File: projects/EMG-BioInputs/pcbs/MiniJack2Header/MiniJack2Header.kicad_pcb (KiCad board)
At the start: 2 copper layers, 22.1 x 14 mm, 2 parts, among them J1 SWITCHCRAFT_35RASMT2BHNTRX, J2 901210124

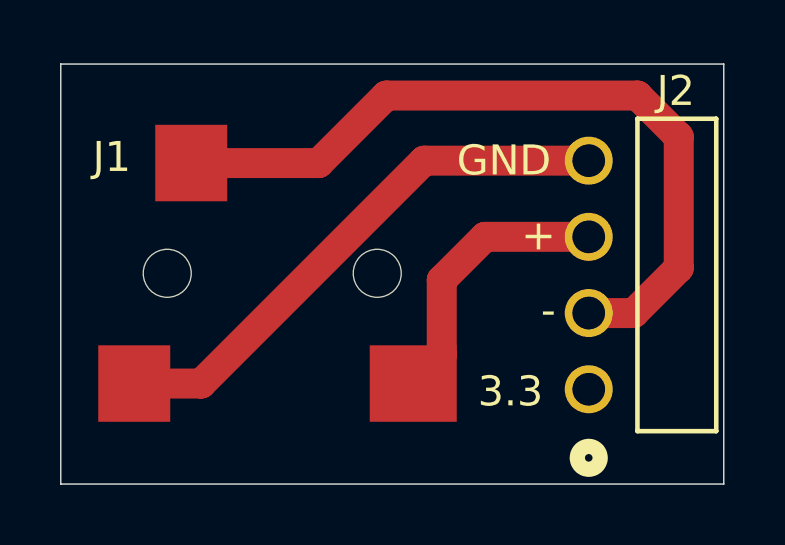
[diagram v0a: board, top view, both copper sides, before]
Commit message: refactor: Rename EMG PCB adapter to Header
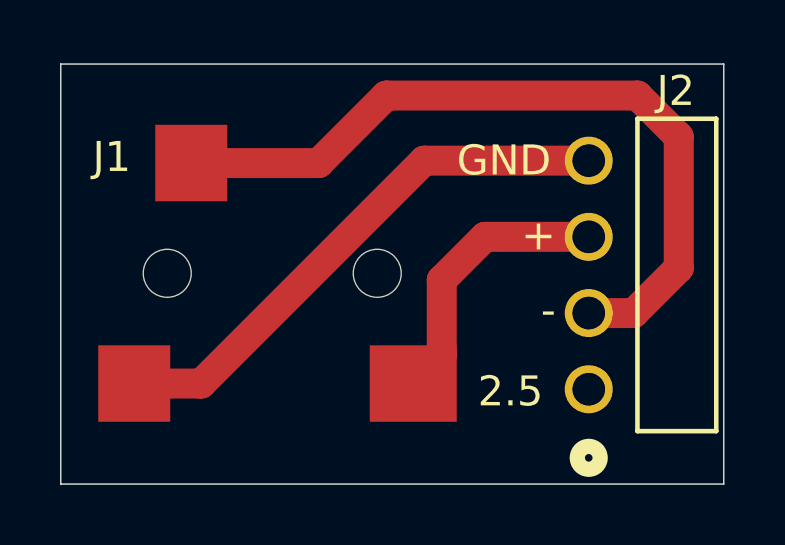
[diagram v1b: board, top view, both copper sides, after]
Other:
- board text added: "2.5"
- board text removed: "3.3"
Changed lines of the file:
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@@
 (kicad_pcb
-	(version 20240108)
+	(version 20241229)
 	(generator "pcbnew")
-	(generator_version "8.0")
+	(generator_version "9.0")
 	(general
 		(thickness 1.6)
@@
 	(layers
 		(0 "F.Cu" signal)
-		(31 "B.Cu" signal)
-		(32 "B.Adhes" user "B.Adhesive")
-		(33 "F.Adhes" user "F.Adhesive")
-		(34 "B.Paste" user)
-		(35 "F.Paste" user)
-		(36 "B.SilkS" user "B.Silkscreen")
-		(37 "F.SilkS" user "F.Silkscreen")
-		(38 "B.Mask" user)
-		(39 "F.Mask" user)
-		(40 "Dwgs.User" user "User.Drawings")
-		(41 "Cmts.User" user "User.Comments")
-		(42 "Eco1.User" user "User.Eco1")
-		(43 "Eco2.User" user "User.Eco2")
-		(44 "Edge.Cuts" user)
-		(45 "Margin" user)
-		(46 "B.CrtYd" user "B.Courtyard")
-		(47 "F.CrtYd" user "F.Courtyard")
-		(48 "B.Fab" user)
-		(49 "F.Fab" user)
-		(50 "User.1" user)
-		(51 "User.2" user)
-		(52 "User.3" user)
-		(53 "User.4" user)
-		(54 "User.5" user)
-		(55 "User.6" user)
-		(56 "User.7" user)
-		(57 "User.8" user)
-		(58 "User.9" user)
+		(2 "B.Cu" signal)
+		(9 "F.Adhes" user "F.Adhesive")
+		(11 "B.Adhes" user "B.Adhesive")
+		(13 "F.Paste" user)
+		(15 "B.Paste" user)
+		(5 "F.SilkS" user "F.Silkscreen")
+		(7 "B.SilkS" user "B.Silkscreen")
+		(1 "F.Mask" user)
+		(3 "B.Mask" user)
+		(17 "Dwgs.User" user "User.Drawings")
+		(19 "Cmts.User" user "User.Comments")
+		(21 "Eco1.User" user "User.Eco1")
+		(23 "Eco2.User" user "User.Eco2")
+		(25 "Edge.Cuts" user)
+		(27 "Margin" user)
+		(31 "F.CrtYd" user "F.Courtyard")
+		(29 "B.CrtYd" user "B.Courtyard")
+		(35 "F.Fab" user)
+		(33 "B.Fab" user)
+		(39 "User.1" user)
+		(41 "User.2" user)
+		(43 "User.3" user)
+		(45 "User.4" user)
+		(47 "User.5" user)
+		(49 "User.6" user)
+		(51 "User.7" user)
+		(53 "User.8" user)
+		(55 "User.9" user)
 	)
 	(setup
@@
 		(pad_to_mask_clearance 0)
 		(allow_soldermask_bridges_in_footprints no)
+		(tenting front back)
 		(pcbplotparams
-			(layerselection 0x00010fc_ffffffff)
-			(plot_on_all_layers_selection 0x0000000_00000000)
+			(layerselection 0x00000000_00000000_55555555_5755f5ff)
+			(plot_on_all_layers_selection 0x00000000_00000000_00000000_00000000)
 			(disableapertmacros no)
 			(usegerberextensions no)
@@
 			(svgprecision 4)
 			(plotframeref no)
-			(viasonmask no)
 			(mode 1)
 			(useauxorigin no)
@@
 			(pdf_front_fp_property_popups yes)
 			(pdf_back_fp_property_popups yes)
+			(pdf_metadata yes)
+			(pdf_single_document no)
 			(dxfpolygonmode yes)
 			(dxfimperialunits yes)
@@
 			(psnegative no)
 			(psa4output no)
-			(plotreference yes)
-			(plotvalue yes)
-			(plotfptext yes)
-			(plotinvisibletext no)
+			(plot_black_and_white yes)
 			(sketchpadsonfab no)
+			(plotpadnumbers no)
+			(hidednponfab no)
+			(sketchdnponfab yes)
+			(crossoutdnponfab yes)
 			(subtractmaskfromsilk no)
 			(outputformat 1)
@@
 			)
 		)
-		(property "Footprint" "MiniJack2Jumper:35RASMT2BHNTRX"
-			(at 0 0 0)
-			(layer "F.Fab")
-			(hide yes)
-			(effects
-				(font
-					(size 1.27 1.27)
-					(thickness 0.15)
-				)
-			)
-		)
 		(property "Datasheet" ""
 			(at 0 0 0)
@@
 				(type default)
 			)
-			(fill none)
+			(fill no)
 			(layer "F.CrtYd")
 		)
@@
 			(size 1.6 1.6)
 			(drill 1.6)
-			(layers "*.Cu" "*.Mask" "In1.Cu" "In2.Cu" "In3.Cu" "In4.Cu" "In5.Cu" "In6.Cu"
-				"In7.Cu" "In8.Cu" "In9.Cu" "In10.Cu" "In11.Cu" "In12.Cu" "In13.Cu" "In14.Cu"
-				"In15.Cu" "In16.Cu" "In17.Cu" "In18.Cu" "In19.Cu" "In20.Cu" "In21.Cu"
-				"In22.Cu" "In23.Cu" "In24.Cu" "In25.Cu" "In26.Cu" "In27.Cu" "In28.Cu"
-				"In29.Cu" "In30.Cu"
-			)
+			(layers "*.Cu" "*.Mask")
 		)
 		(pad "" np_thru_hole circle
@@
 			(size 1.6 1.6)
 			(drill 1.6)
-			(layers "*.Cu" "*.Mask" "In1.Cu" "In2.Cu" "In3.Cu" "In4.Cu" "In5.Cu" "In6.Cu"
-				"In7.Cu" "In8.Cu" "In9.Cu" "In10.Cu" "In11.Cu" "In12.Cu" "In13.Cu" "In14.Cu"
-				"In15.Cu" "In16.Cu" "In17.Cu" "In18.Cu" "In19.Cu" "In20.Cu" "In21.Cu"
-				"In22.Cu" "In23.Cu" "In24.Cu" "In25.Cu" "In26.Cu" "In27.Cu" "In28.Cu"
-				"In29.Cu" "In30.Cu"
-			)
+			(layers "*.Cu" "*.Mask")
 		)
 		(pad "1" smd rect
 			(at -2.7 -3.675)
 			(size 2.4 2.55)
-			(layers "F.Cu" "F.Paste" "F.Mask")
+			(layers "F.Cu" "F.Mask" "F.Paste")
 			(net 3 "/-IN")
 			(pinfunction "1")
@@
 			(at 4.7 3.675)
 			(size 2.9 2.55)
-			(layers "F.Cu" "F.Paste" "F.Mask")
+			(layers "F.Cu" "F.Mask" "F.Paste")
 			(net 1 "/+IN")
 			(pinfunction "4")
@@
 			(at -4.6 3.675)
 			(size 2.4 2.55)
-			(layers "F.Cu" "F.Paste" "F.Mask")
+			(layers "F.Cu" "F.Mask" "F.Paste")
 			(net 2 "/GND")
 			(pinfunction "5")
@@
 			(solder_mask_margin 0.102)
 		)
+		(embedded_fonts no)
 		(model "${KIPRJMOD}/libraries/3dmodels/35RASMT2BHNTRX.step"
 			(offset
@@
 			)
 		)
-		(property "Footprint" "MiniJack2Jumper:CONN04_901210124_MOL"
-			(at 0 0 90)
-			(layer "F.Fab")
-			(hide yes)
-			(effects
-				(font
-					(size 1.27 1.27)
-					(thickness 0.15)
-				)
-			)
-		)
 		(property "Datasheet" "https://www.molex.com/pdm_docs/sd/901210124_sd.pdf"
 			(at 0 0 90)
@@
 		(sheetfile "MiniJack2Jumper.kicad_sch")
 		(attr through_hole)
+		(fp_line
+			(start 9.017 1.62306)
+			(end -1.397 1.62306)
+			(stroke
+				(width 0.1524)
+				(type solid)
+			)
+			(layer "F.SilkS")
+		)
+		(fp_line
+			(start -1.397 1.62306)
+			(end -1.397 4.25)
+			(stroke
+				(width 0.1524)
+				(type solid)
+			)
+			(layer "F.SilkS")
+		)
+		(fp_line
+			(start 9.017 4.25)
+			(end 9.017 1.62306)
+			(stroke
+				(width 0.1524)
+				(type solid)
+			)
+			(layer "F.SilkS")
+		)
+		(fp_line
+			(start -1.397 4.25)
+			(end 9.017 4.25)
+			(stroke
+				(width 0.1524)
+				(type solid)
+			)
+			(layer "F.SilkS")
+		)
 		(fp_circle
 			(center -2.286 0)
@@
 				(type solid)
 			)
-			(fill none)
-			(layer "B.SilkS")
-		)
-		(fp_line
-			(start 9.017 1.62306)
-			(end -1.397 1.62306)
-			(stroke
-				(width 0.1524)
-				(type solid)
-			)
-			(layer "F.SilkS")
-		)
-		(fp_line
-			(start -1.397 1.62306)
-			(end -1.397 4.25)
-			(stroke
-				(width 0.1524)
-				(type solid)
-			)
-			(layer "F.SilkS")
-		)
-		(fp_line
-			(start 9.017 4.25)
-			(end 9.017 1.62306)
-			(stroke
-				(width 0.1524)
-				(type solid)
-			)
-			(layer "F.SilkS")
-		)
-		(fp_line
-			(start -1.397 4.25)
-			(end 9.017 4.25)
-			(stroke
-				(width 0.1524)
-				(type solid)
-			)
+			(fill no)
 			(layer "F.SilkS")
 		)
@@
 				(type solid)
 			)
-			(fill none)
-			(layer "F.SilkS")
+			(fill no)
+			(layer "B.SilkS")
 		)
 		(fp_line
@@
 				(type solid)
 			)
-			(fill none)
+			(fill no)
 			(layer "F.Fab")
 		)
@@
 			(size 1.6002 1.6002)
 			(drill 1.0922)
-			(layers "*.Cu" "*.Mask" "In1.Cu" "In2.Cu" "In3.Cu" "In4.Cu" "In5.Cu" "In6.Cu"
-				"In7.Cu" "In8.Cu" "In9.Cu" "In10.Cu" "In11.Cu" "In12.Cu" "In13.Cu" "In14.Cu"
-				"In15.Cu" "In16.Cu" "In17.Cu" "In18.Cu" "In19.Cu" "In20.Cu" "In21.Cu"
-				"In22.Cu" "In23.Cu" "In24.Cu" "In25.Cu" "In26.Cu" "In27.Cu" "In28.Cu"
-				"In29.Cu" "In30.Cu"
-			)
+			(layers "*.Cu" "*.Mask")
 			(remove_unused_layers no)
 			(net 4 "unconnected-(J2-Pad1)")
@@
 			(size 1.6002 1.6002)
 			(drill 1.0922)
-			(layers "*.Cu" "*.Mask" "In1.Cu" "In2.Cu" "In3.Cu" "In4.Cu" "In5.Cu" "In6.Cu"
-				"In7.Cu" "In8.Cu" "In9.Cu" "In10.Cu" "In11.Cu" "In12.Cu" "In13.Cu" "In14.Cu"
-				"In15.Cu" "In16.Cu" "In17.Cu" "In18.Cu" "In19.Cu" "In20.Cu" "In21.Cu"
-				"In22.Cu" "In23.Cu" "In24.Cu" "In25.Cu" "In26.Cu" "In27.Cu" "In28.Cu"
-				"In29.Cu" "In30.Cu"
-			)
+			(layers "*.Cu" "*.Mask")
 			(remove_unused_layers no)
 			(net 3 "/-IN")
@@
 			(size 1.6002 1.6002)
 			(drill 1.0922)
-			(layers "*.Cu" "*.Mask" "In1.Cu" "In2.Cu" "In3.Cu" "In4.Cu" "In5.Cu" "In6.Cu"
-				"In7.Cu" "In8.Cu" "In9.Cu" "In10.Cu" "In11.Cu" "In12.Cu" "In13.Cu" "In14.Cu"
-				"In15.Cu" "In16.Cu" "In17.Cu" "In18.Cu" "In19.Cu" "In20.Cu" "In21.Cu"
-				"In22.Cu" "In23.Cu" "In24.Cu" "In25.Cu" "In26.Cu" "In27.Cu" "In28.Cu"
-				"In29.Cu" "In30.Cu"
-			)
+			(layers "*.Cu" "*.Mask")
 			(remove_unused_layers no)
 			(net 1 "/+IN")
@@
 			(size 1.6002 1.6002)
 			(drill 1.0922)
-			(layers "*.Cu" "*.Mask" "In1.Cu" "In2.Cu" "In3.Cu" "In4.Cu" "In5.Cu" "In6.Cu"
-				"In7.Cu" "In8.Cu" "In9.Cu" "In10.Cu" "In11.Cu" "In12.Cu" "In13.Cu" "In14.Cu"
-				"In15.Cu" "In16.Cu" "In17.Cu" "In18.Cu" "In19.Cu" "In20.Cu" "In21.Cu"
-				"In22.Cu" "In23.Cu" "In24.Cu" "In25.Cu" "In26.Cu" "In27.Cu" "In28.Cu"
-				"In29.Cu" "In30.Cu"
-			)
+			(layers "*.Cu" "*.Mask")
 			(remove_unused_layers no)
 			(net 2 "/GND")
@@
 			(pintype "unspecified")
 		)
+		(embedded_fonts no)
 		(model "${KIPRJMOD}/libraries/3dmodels/CONN04_901210124_MOL.stp"
 			(offset
@@
 			(type default)
 		)
-		(fill none)
+		(fill no)
 		(layer "Edge.Cuts")
 	)
-	(gr_text "3.3"
+	(gr_text "2.5"
 		(at 139.3 100.2 0)
 		(layer "F.SilkS")
@@
 		(net 3)
 	)
+	(embedded_fonts no)
 )

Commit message: fix: Change header pin layout for SensEdu 0.8+
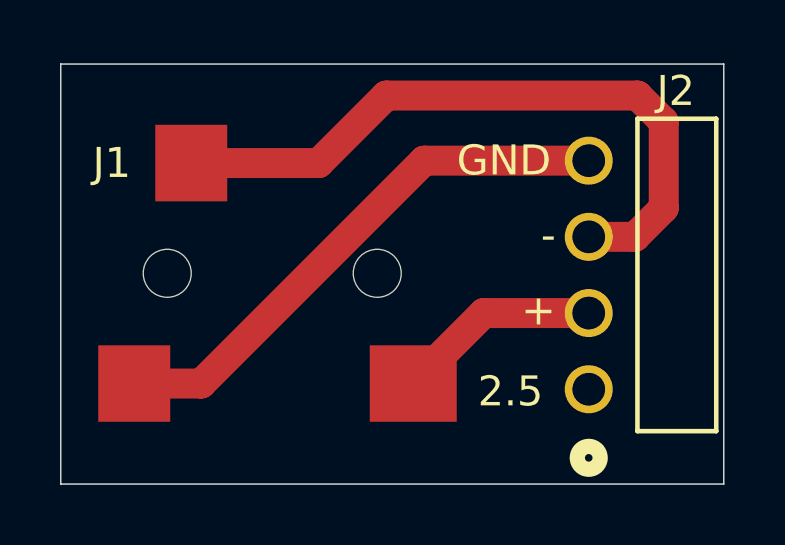
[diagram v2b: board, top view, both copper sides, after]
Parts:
- J1: value SWITCHCRAFT_35RASMT2BHNTRX -> 35RASMT2BHNTRX; footprint MiniJack2Jumper:35RASMT2BHNTRX -> MiniJack2Header:35RASMT2BHNTRX
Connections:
- J2 pad 2: /-IN -> /+IN
- J2 pad 3: /+IN -> /-IN
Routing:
- net /-IN: track 25.7 -> 22.8 mm
- net /+IN: track 9.34 -> 6.82 mm
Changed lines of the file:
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@@
 	(net 3 "/-IN")
 	(net 4 "unconnected-(J2-Pad1)")
-	(footprint "MiniJack2Jumper:35RASMT2BHNTRX"
+	(footprint "MiniJack2Header:35RASMT2BHNTRX"
 		(layer "F.Cu")
 		(at 132.45 95.675)
 		(property "Reference" "J1"
-			(at -5.35 -3.875 0)
+			(at -5.35 -3.675 0)
 			(layer "F.SilkS")
 			(effects
@@
 			)
 		)
-		(property "Value" "SWITCHCRAFT_35RASMT2BHNTRX"
+		(property "Value" "35RASMT2BHNTRX"
 			(at 10.52252 6.372545 0)
 			(layer "F.Fab")
@@
 			)
 		)
-		(property "Datasheet" ""
+		(property "Datasheet" "https://www.switchcraft.com/assets/1/24/35rasmt2bhntrx_cd.pdf?4698"
 			(at 0 0 0)
 			(layer "F.Fab")
@@
 			)
 		)
-		(sheetname "Root")
-		(sheetfile "MiniJack2Jumper.kicad_sch")
+		(property "DigiKey Part Number" "SC1489-1-ND"
+			(at 0 0 0)
+			(unlocked yes)
+			(layer "F.Fab")
+			(hide yes)
+			(effects
+				(font
+					(size 1 1)
+					(thickness 0.15)
+				)
+			)
+		)
+		(property "DigiKey Link" "https://www.digikey.at/en/products/detail/switchcraft-inc/35RASMT2BHNTRX/1291178"
+			(at 0 0 0)
+			(unlocked yes)
+			(layer "F.Fab")
+			(hide yes)
+			(effects
+				(font
+					(size 1 1)
+					(thickness 0.15)
+				)
+			)
+		)
+		(sheetname "/")
+		(sheetfile "MiniJack2Header.kicad_sch")
 		(attr smd)
 		(fp_rect
@@
 		)
 		(property ki_fp_filters "CONN04_901210124_MOL")
-		(sheetname "Root")
-		(sheetfile "MiniJack2Jumper.kicad_sch")
+		(sheetname "/")
+		(sheetfile "MiniJack2Header.kicad_sch")
 		(attr through_hole)
 		(fp_line
@@
 			(layers "*.Cu" "*.Mask")
 			(remove_unused_layers no)
-			(net 3 "/-IN")
+			(net 1 "/+IN")
 			(pinfunction "2")
 			(pintype "unspecified")
@@
 			(layers "*.Cu" "*.Mask")
 			(remove_unused_layers no)
-			(net 1 "/+IN")
+			(net 3 "/-IN")
 			(pinfunction "3")
 			(pintype "unspecified")
@@
 		)
 	)
-	(gr_text "+"
+	(gr_text "-"
 		(at 141.9 95 0)
 		(layer "F.SilkS")
@@
 		)
 	)
-	(gr_text "-"
+	(gr_text "+"
 		(at 141.9 97.5 0)
 		(layer "F.SilkS")
@@
 	)
 	(segment
-		(start 138.1 98.4)
+		(start 143 97)
+		(end 139.5 97)
+		(width 1)
+		(layer "F.Cu")
+		(net 1)
+	)
+	(segment
+		(start 139.5 97)
 		(end 137.15 99.35)
-		(width 1)
-		(layer "F.Cu")
-		(net 1)
-	)
-	(segment
-		(start 138.1 95.9)
-		(end 138.1 98.4)
-		(width 1)
-		(layer "F.Cu")
-		(net 1)
-	)
-	(segment
-		(start 139.54 94.46)
-		(end 138.1 95.9)
-		(width 1)
-		(layer "F.Cu")
-		(net 1)
-	)
-	(segment
-		(start 143 94.46)
-		(end 139.54 94.46)
 		(width 1)
 		(layer "F.Cu")
@@
 	)
 	(segment
+		(start 145.5 90.625)
+		(end 145.5 93.5)
+		(width 1)
+		(layer "F.Cu")
+		(net 3)
+	)
+	(segment
+		(start 144.54 94.46)
+		(end 143 94.46)
+		(width 1)
+		(layer "F.Cu")
+		(net 3)
+	)
+	(segment
+		(start 136.25 89.75)
+		(end 144.625 89.75)
+		(width 1)
+		(layer "F.Cu")
+		(net 3)
+	)
+	(segment
+		(start 145.5 93.5)
+		(end 144.54 94.46)
+		(width 1)
+		(layer "F.Cu")
+		(net 3)
+	)
+	(segment
+		(start 144.625 89.75)
+		(end 145.5 90.625)
+		(width 1)
+		(layer "F.Cu")
+		(net 3)
+	)
+	(segment
+		(start 129.75 92)
+		(end 134 92)
+		(width 1)
+		(layer "F.Cu")
+		(net 3)
+	)
+	(segment
 		(start 134 92)
-		(end 129.75 92)
-		(width 1)
-		(layer "F.Cu")
-		(net 3)
-	)
-	(segment
-		(start 146 95.5)
-		(end 146 91.125)
-		(width 1)
-		(layer "F.Cu")
-		(net 3)
-	)
-	(segment
-		(start 143 97)
-		(end 144.5 97)
-		(width 1)
-		(layer "F.Cu")
-		(net 3)
-	)
-	(segment
-		(start 144.625 89.75)
 		(end 136.25 89.75)
 		(width 1)
 		(layer "F.Cu")
-		(net 3)
-	)
-	(segment
-		(start 136.25 89.75)
-		(end 134 92)
-		(width 1)
-		(layer "F.Cu")
-		(net 3)
-	)
-	(segment
-		(start 144.5 97)
-		(end 146 95.5)
-		(width 1)
-		(layer "F.Cu")
-		(net 3)
-	)
-	(segment
-		(start 146 91.125)
-		(end 144.625 89.75)
-		(width 1)
-		(layer "F.Cu")
